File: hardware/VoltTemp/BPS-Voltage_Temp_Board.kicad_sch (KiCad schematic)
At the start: 14 parts, among them J10 53307-2471, J12 Conn_01x04, J13 Conn_01x04, J2 PeripheralCAN, J5 Logic_Analyzer

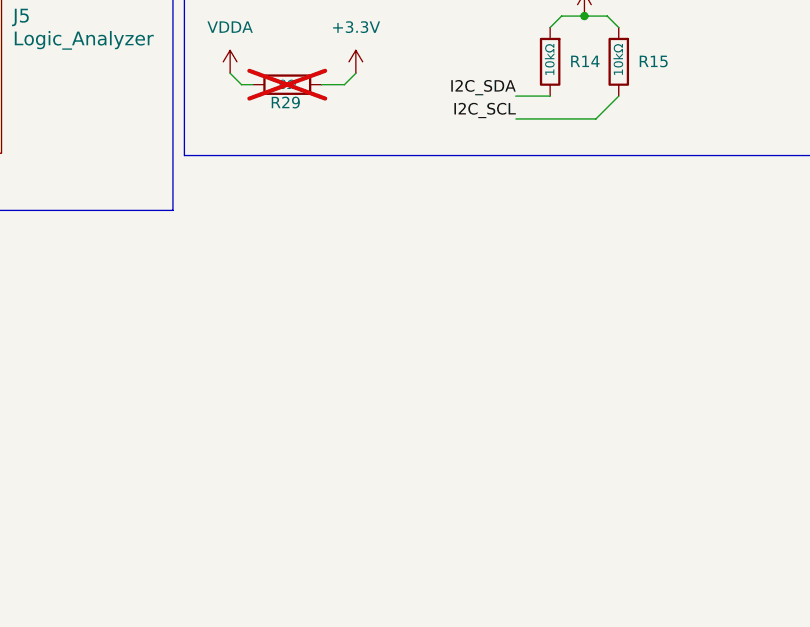
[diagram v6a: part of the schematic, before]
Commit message: voltage testpoints
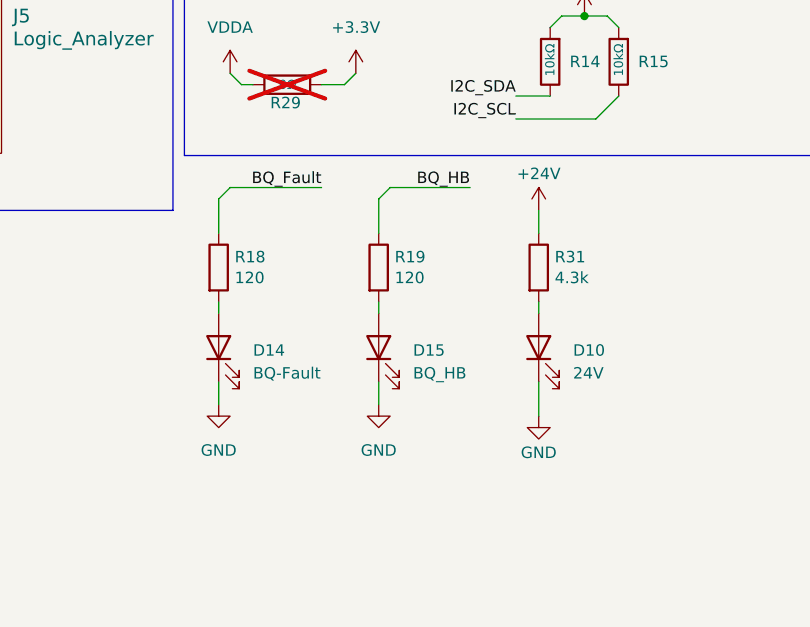
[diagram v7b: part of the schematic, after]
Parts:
- added D10: 24V, LED_SMD:LED_0603_1608Metric_Pad1.05x0.95mm_HandSolder, symbol Device:LED
- added D14: BQ-Fault, LED_SMD:LED_0603_1608Metric_Pad1.05x0.95mm_HandSolder, symbol Device:LED
- added D15: BQ_HB, LED_SMD:LED_0603_1608Metric_Pad1.05x0.95mm_HandSolder, symbol Device:LED
- added R18, R19: 120, Resistor_SMD:R_0603_1608Metric_Pad0.98x0.95mm_HandSolder, symbol Device:R
- added R31: 4.3k, Resistor_SMD:R_0603_1608Metric_Pad0.98x0.95mm_HandSolder, symbol Device:R
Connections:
- net +24V: now also R31.1
- net GND: now also D10.1 (K), D14.1 (K), D15.1 (K)
- new net: D14.2 (A), R18.2
- new net: D15.2 (A), R19.2
- new net: D10.2 (A), R31.2
- new net BQ_Fault: R18.1
- new net BQ_HB: R19.1

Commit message: done except for nanofit footprints
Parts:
- added TP2, TP5: TestPoint, TestPoint:TestPoint_Pad_1.0x1.0mm, symbol Connector:TestPoint
- D10: value 24V -> 3v3
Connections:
- net +24V: no longer R31.1
- net +3.3V: now also R31.1, TP2.1
- net BQ_Fault: now also J10.21 (SPI1_MISO)
- net BQ_HB: now also J10.17 (SPI1_MOSI)
- net GND: now also TP5.1
- no-connect marks 14 -> 12
